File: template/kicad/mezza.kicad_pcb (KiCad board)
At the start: 2 copper layers, 85 x 54 mm, 6 parts, among them P1 CONN_02X20, P2 CONN_02X20

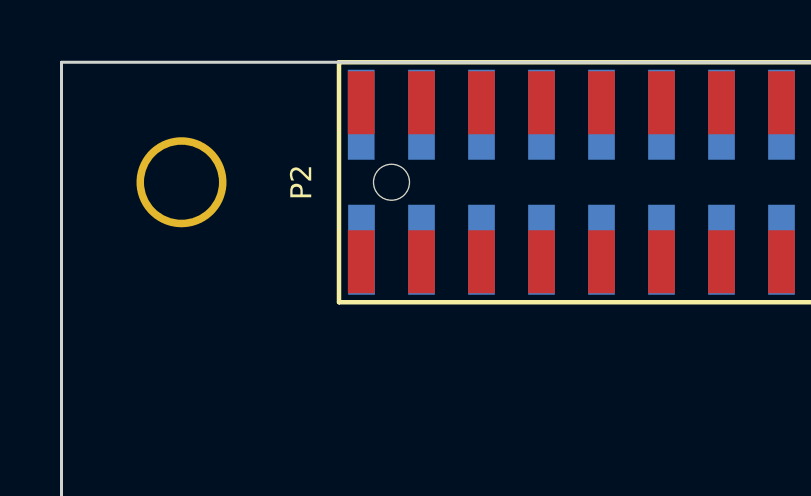
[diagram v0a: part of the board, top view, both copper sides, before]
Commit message: Adjust SMT header patterns
The first few pins were very slightly misaligned.

Signed-off-by: Michael Welling <mwelling@ieee.org>
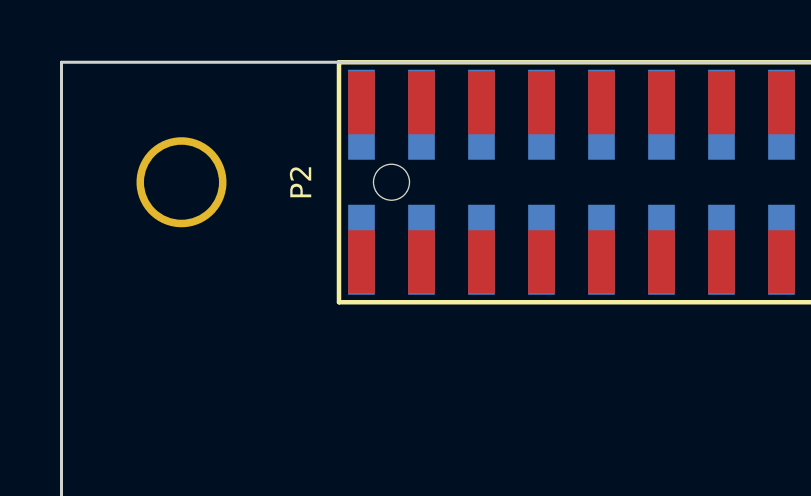
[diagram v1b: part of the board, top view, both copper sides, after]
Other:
- net class Default: clearance 0.1778 -> 0
- rule trace_clearance: 0.1778 -> 0
